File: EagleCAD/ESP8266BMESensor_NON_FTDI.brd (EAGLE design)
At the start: 55 x 30 mm, 21 parts, among them J1 AMP FCI 10103594-0001LF

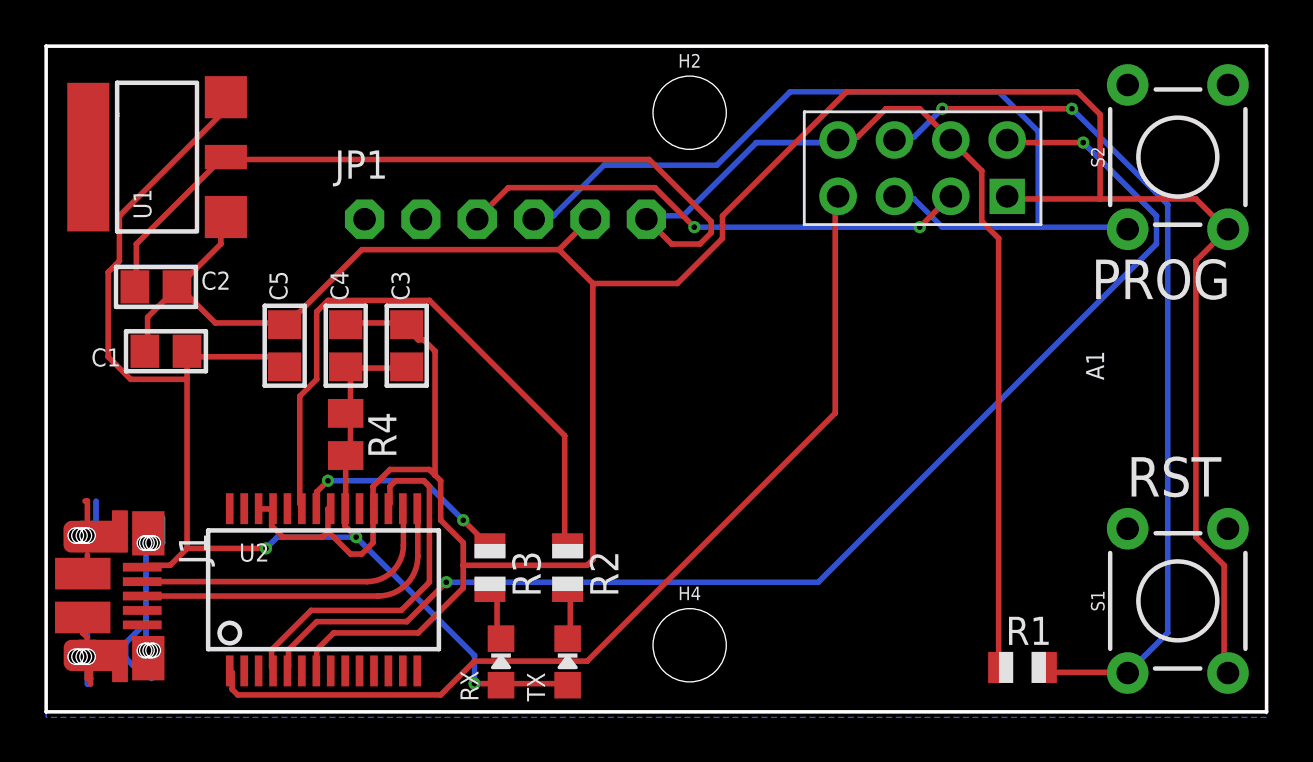
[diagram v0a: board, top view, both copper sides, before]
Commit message: adding back the FTDI version as the primary
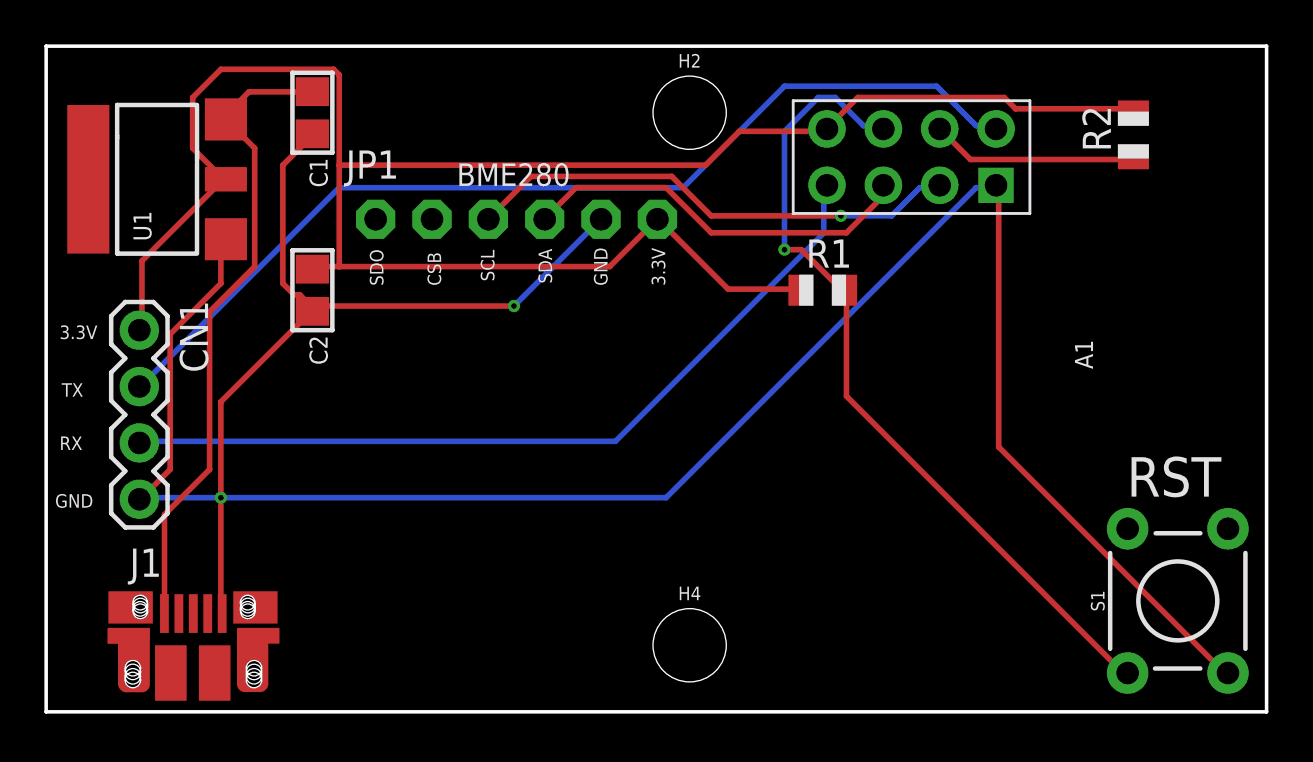
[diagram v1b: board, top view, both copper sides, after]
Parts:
- removed C3: 0.1uF, microbuilder:0805
- removed C4: 10uF, microbuilder:0805
- removed C5: 0.01uF, microbuilder:0805
- removed R3: 330 OHM, adafruit:R0805
- removed R4: FERRITE BEAD, adafruit:M0805
- removed RX, TX: (no value), microbuilder:CHIPLED_0805_NOOUTLINE
- removed S2: MOMENTARY-SWITCH-SPST-PTH-6.0MM, SparkFun-Switches:TACTILE_SWITCH_PTH_6.0MM
- removed U2: (no value), microbuilder:SSOP28DB
- added CN1: 1X4-BIG, adafruit:1X04-BIG
- R2: value 330 OHM -> (none)
- moved R2 32.1 mm to (49.0, 26.0), turned to 90 degrees
- moved R1 19.2 mm to (35.0, 19.0)
- moved C1 12.6 mm to (12.0, 27.0), turned to 270 degrees
- moved C2 7.05 mm to (12.0, 19.0), turned to 270 degrees
- moved J1 4.19 mm to (6.60, 3.10), turned to 0 degrees
- moved U1 1.00 mm to (5.00, 24.0)
- moved A1 0.71 mm to (39.0, 25.0)
- moved JP1 0.50 mm to (21.2, 22.2)
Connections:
- removed net N$2: R2.2, TX.C
- removed net N$3: R3.2, RX.C
- removed net RXLED: R3.1, U2.22
- removed net TXLED: R2.1, U2.23
- removed net USB+: J1.D+, U2.15
- removed net USB-: J1.D-, U2.16
- removed net VCCIO: U2.17, U2.4
- new net EN/CHPD: A1.EN/CH_PD, R2.1
- net +5V: no longer C3.1, C4.1, C5.1, R4.1, R4.2, RX.A, TX.A, U2.20
- net 3.3V: now also CN1.1, R2.2; no longer A1.EN/CH_PD
- net GND: now also CN1.4; no longer C3.2, C4.2, C5.2, J1.P$1, J1.P$10, J1.P$12, J1.P$2, J1.P$3, J1.P$4, J1.P$6, J1.P$8, J1.SHEILD2, J1.SHIELD, J1.SHIELD3, J1.SHIELD4, S2.3, U2.18, U2.21, U2.25, U2.26, U2.7
- net RX: now also CN1.3; no longer U2.1
- net SDA: no longer S2.1
- net TX: now also CN1.2; no longer U2.5
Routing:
- net GND: track 173.0 -> 123.5 mm, vias 0 -> 2
- net +5V: track 65.8 -> 29.0 mm, vias 3 -> 0
- net TXLED: track 28.1 -> 0.00 mm
- net SDA: track 41.3 -> 17.9 mm
- net VCCIO: track 16.7 -> 0.00 mm
- net USB+: track 15.3 -> 0.00 mm
- net 3.3V: track 75.9 -> 90.2 mm
- net USB-: track 14.1 -> 0.00 mm
- net TX: track 57.1 -> 45.0 mm, vias 2 -> 0
- net RXLED: track 9.96 -> 0.00 mm, vias 2 -> 0
- net EN/CHPD: track 0.00 -> 9.32 mm
- net RX: track 43.3 -> 37.0 mm
- net RST: track 40.4 -> 37.1 mm, vias 2 -> 1
- net N$3: track 2.50 -> 0.00 mm
- net N$2: track 2.36 -> 0.00 mm
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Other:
- board text added: "3.3V"
- board text added: "BME280"
- board text added: "CSB"
- board text added: "GND"
- board text added: "RX"
- board text added: "SCL"
- board text added: "SDA"
- board text added: "SDO"
- board text added: "TX"
- board text added: "v1.5"
- board text removed: "PROG"
- board text removed: "v1.4"
